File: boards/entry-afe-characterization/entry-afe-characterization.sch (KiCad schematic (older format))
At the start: 0 parts

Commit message: Continued design of entry-afe-characterization
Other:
- note added: "SYSTEM GAIN CALCULATIONS\n\nHMCAD1520 wants 2V full scale\nIn 12-bit mode: 488 µV/LSB @ 0 dB gain\nIn 8-bit mode: 7.8 mV/LSB @ 0 dB gain\n\nMIN GAIN:\n10V input range, -13 dB system gain (0.2V/V)\n-9 dB gain on VGA\n12 bit mode: 2.4 mV/LSB\n8 bit mode: 39 mV/LSB\n\nMAX GAIN:\n159 mV input range, +22 dB system gain (12.59V/V)\n+26 dB gain on VGA\n12 bit mode: 38.7 µV/LSB\n8 bit mode: 619.5 µV/LSB"
- note added: "VGAIN\n2.5V CM\nNet gain = 0.177 - 10 V/V\n-15 to +20 dB"
- note added: "VOUT\n900 mV CM\nNet gain = 0.223 - 12.59 V/V\n-13 to +22 dB"
- note removed: "SYSTEM GAIN CALCULATIONS\n\nHMCAD1520 wants 2V full scale\nIn 12-bit mode: 488 µV/LSB @ 0 dB gain\nIn 8-bit mode: 7.8 mV/LSB @ 0 dB gain\n\nMIN GAIN:\n10V input range, -13 dB system gain (0.2V/V)\n+2 dB gain on VGA\n12 bit mode: 2.4 mV/LSB\n8 bit mode: 39 mV/LSB\n\nMAX GAIN:\n502 mV input range, +12 dB system gain (3.98V/V)\n+26 dB gain on VGA\n12 bit mode: 122.6 µV/LSB\n8 bit mode: 1.95 mV/LSB"
- note removed: "VGAIN\n2.25V CM\nNet gain = 0.177 - 10 V/V\n-15 to +20 dB"
- note removed: "VOUT\n895 mV CM\nNet gain = 0.071 - 3.98 V/V\n-23 to +12 dB"
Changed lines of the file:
@@
 $EndSheet
 Text Notes 6350 3850 0    50   ~ 0
-SYSTEM GAIN CALCULATIONS\n\nHMCAD1520 wants 2V full scale\nIn 12-bit mode: 488 µV/LSB @ 0 dB gain\nIn 8-bit mode: 7.8 mV/LSB @ 0 dB gain\n\nMIN GAIN:\n10V input range, -13 dB system gain (0.2V/V)\n+2 dB gain on VGA\n12 bit mode: 2.4 mV/LSB\n8 bit mode: 39 mV/LSB\n\nMAX GAIN:\n502 mV input range, +12 dB system gain (3.98V/V)\n+26 dB gain on VGA\n12 bit mode: 122.6 µV/LSB\n8 bit mode: 1.95 mV/LSB
+SYSTEM GAIN CALCULATIONS\n\nHMCAD1520 wants 2V full scale\nIn 12-bit mode: 488 µV/LSB @ 0 dB gain\nIn 8-bit mode: 7.8 mV/LSB @ 0 dB gain\n\nMIN GAIN:\n10V input range, -13 dB system gain (0.2V/V)\n-9 dB gain on VGA\n12 bit mode: 2.4 mV/LSB\n8 bit mode: 39 mV/LSB\n\nMAX GAIN:\n159 mV input range, +22 dB system gain (12.59V/V)\n+26 dB gain on VGA\n12 bit mode: 38.7 µV/LSB\n8 bit mode: 619.5 µV/LSB
 $Sheet
 S 3900 5500 650  1750
@@
 F5 "VGAIN_P" O R 5650 750 50
 F6 "VGAIN_N" O R 5650 850 50
-F7 "2V25_REF" I L 4500 1150 50
+F7 "2V5_REF" I L 4500 1150 50
 $EndSheet
 Wire Wire Line
@@
 VSHIFTED\n0-5V range, 2.5V CM\nNet gain = 0.5V/V (-6 dB)\nVIN_OFFSET is ± 2.5V range
 Text Notes 4500 2050 0    50   ~ 0
-VGAIN\n2.25V CM\nNet gain = 0.177 - 10 V/V\n-15 to +20 dB
+VGAIN\n2.5V CM\nNet gain = 0.177 - 10 V/V\n-15 to +20 dB
 Text Label 4500 1150 2    50   ~ 0
-2V25_REF
+2V5_REF
 $Sheet
 S 6350 650  950  950
@@
 F2 "VGAIN_P" I L 6350 750 50
 F3 "VGAIN_N" I L 6350 850 50
-F4 "GND" I L 6350 1050 50
-F6 "VOUT_P" O R 7300 750 50
-F7 "VOUT_N" O R 7300 850 50
+F4 "GND" I L 6350 1150 50
+F5 "VOUT_P" O R 7300 750 50
+F6 "VOUT_N" O R 7300 850 50
+F7 "0V9_REF" I L 6350 1050 50
 $EndSheet
 Wire Wire Line
@@
 Wire Wire Line
 	5650 850  6350 850
-Text Label 6350 1050 2    50   ~ 0
+Text Label 6350 1150 2    50   ~ 0
 GND
 Text Notes 6350 2050 0    50   ~ 0
-VOUT\n895 mV CM\nNet gain = 0.071 - 3.98 V/V\n-23 to +12 dB
+VOUT\n900 mV CM\nNet gain = 0.223 - 12.59 V/V\n-13 to +22 dB
+Text Label 6350 1050 2    50   ~ 0
+0V9_REF
 $EndSCHEMATC

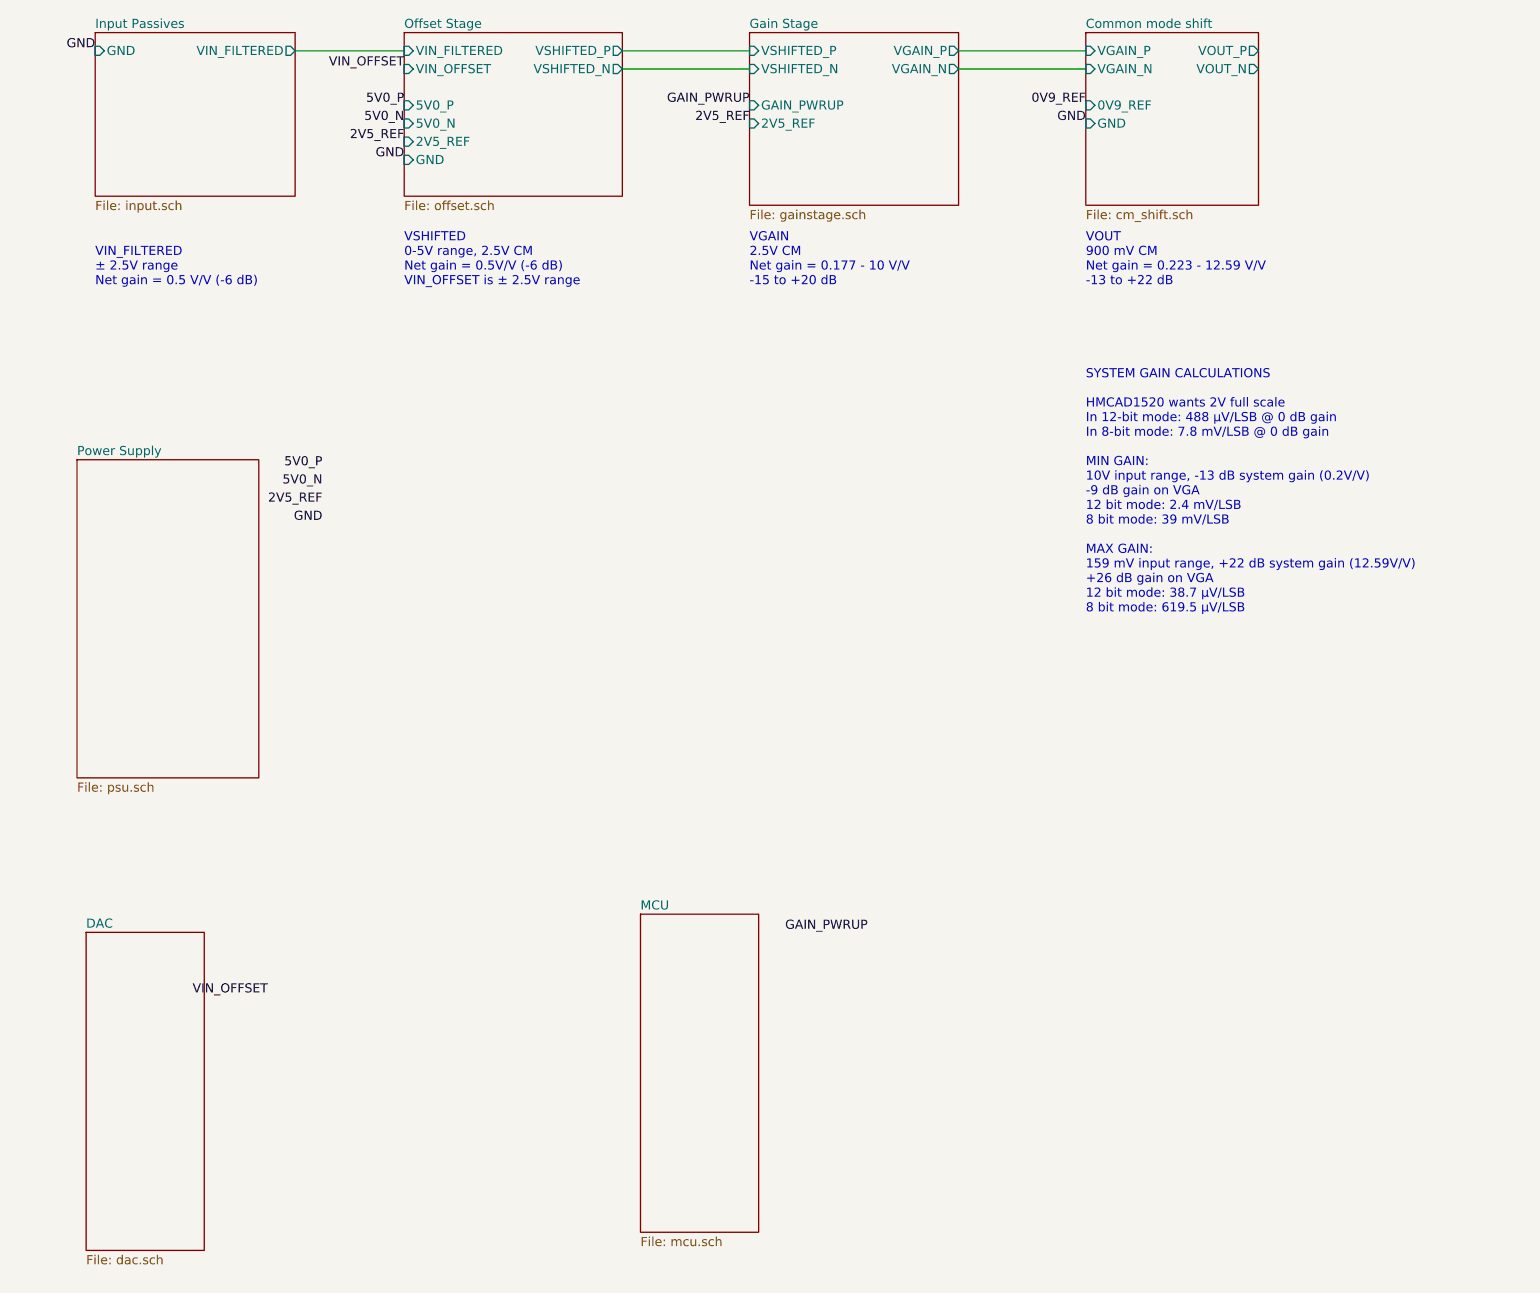
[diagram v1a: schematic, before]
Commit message: Continued work on AFE characterization board
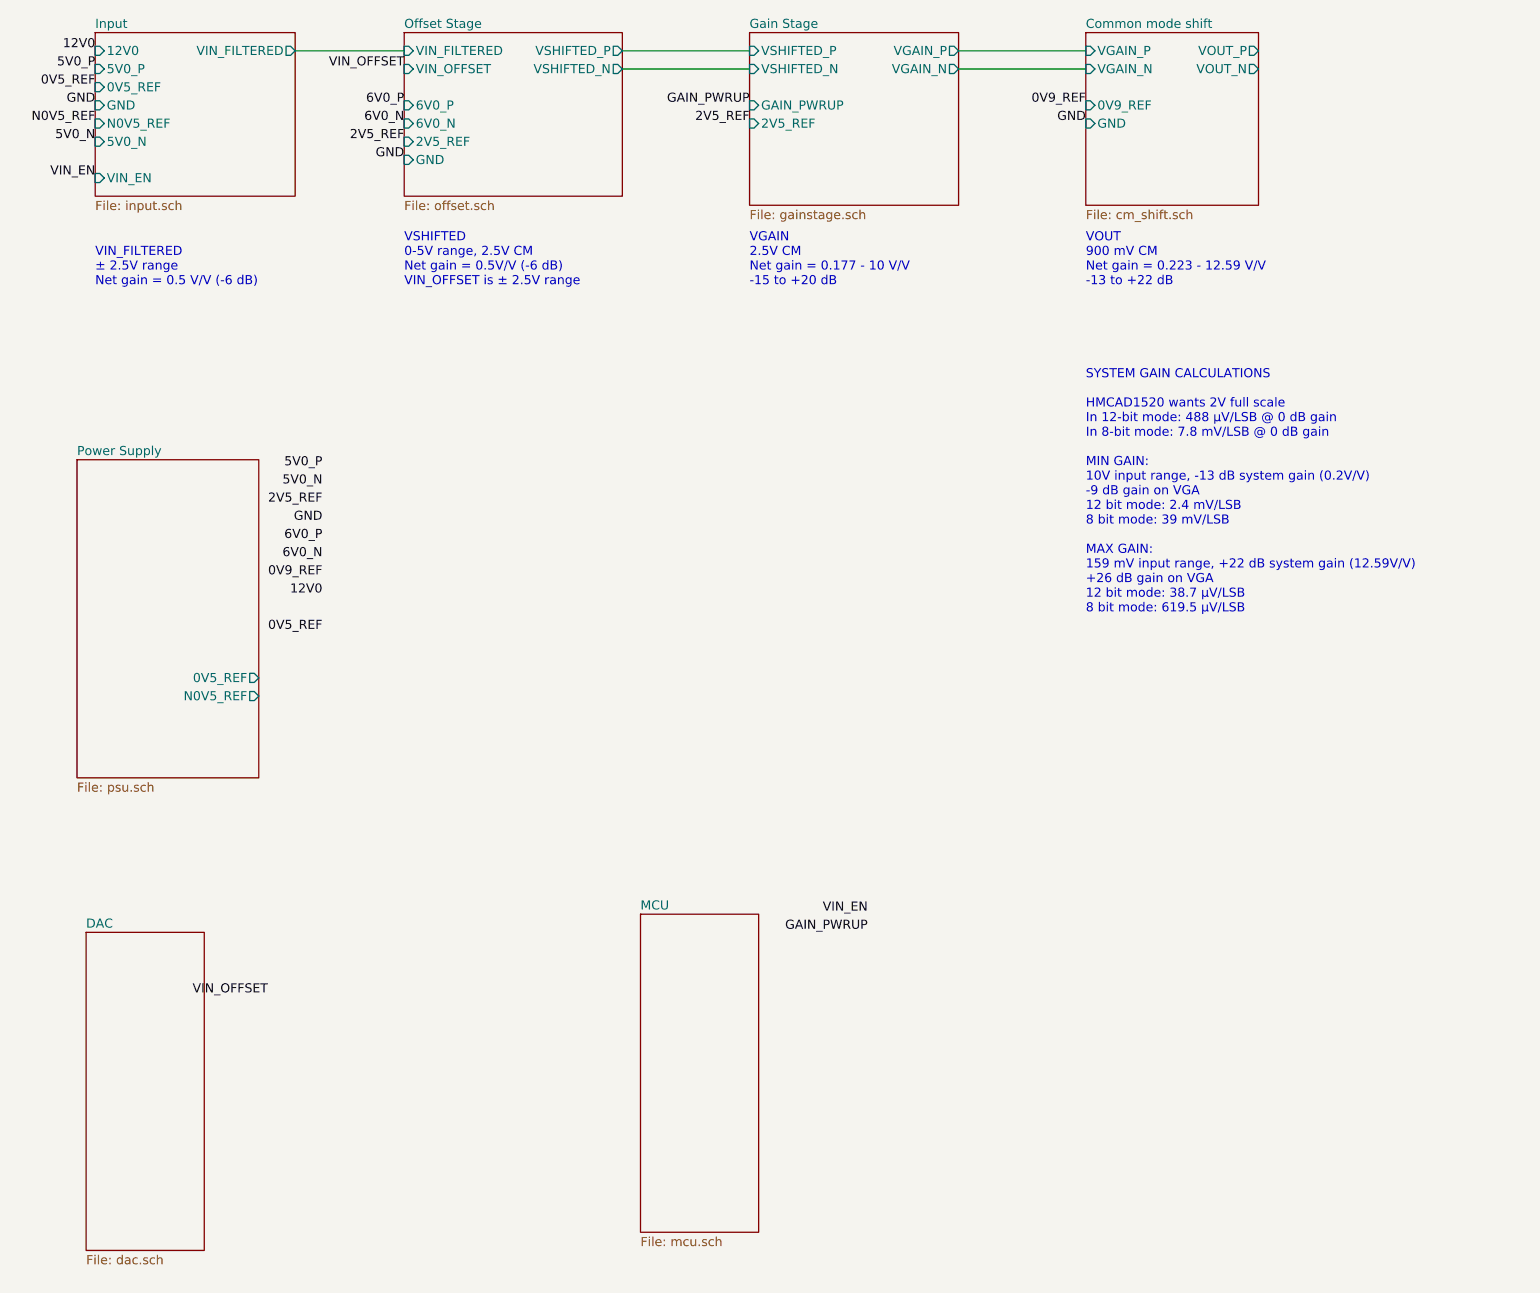
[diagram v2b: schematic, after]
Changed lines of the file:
@@
 EESchema Schematic File Version 4
+LIBS:entry-afe-characterization-cache
 EELAYER 30 0
 EELAYER END
@@
 Sheet 1 8
 Title "Entry-Level Oscilloscope AFE Characterization Platform"
-Date "2020-03-16"
+Date "2020-03-17"
 Rev "0.1"
 Comp "Antikernel Labs"
@@
 F0 "Power Supply" 50
 F1 "psu.sch" 50
+F2 "0V5_REF" O R 1800 4200 50
+F3 "N0V5_REF" O R 1800 4300 50
 $EndSheet
 $Sheet
@@
 S 900  650  1100 900
 U 5E7383DD
-F0 "Input Passives" 50
+F0 "Input" 50
 F1 "input.sch" 50
-F2 "GND" I L 900 750 50
+F2 "GND" I L 900 1050 50
 F3 "VIN_FILTERED" O R 2000 750 50
+F4 "VIN_EN" I L 900 1450 50
+F5 "5V0_P" I L 900 850 50
+F6 "5V0_N" I L 900 1250 50
+F7 "12V0" I L 900 750 50
+F8 "0V5_REF" I L 900 950 50
+F9 "N0V5_REF" I L 900 1150 50
 $EndSheet
-Text Label 900  750  2    50   ~ 0
+Text Label 900  1050 2    50   ~ 0
 GND
 $Sheet
@@
 F4 "VSHIFTED_P" O R 3800 750 50
 F5 "VSHIFTED_N" O R 3800 850 50
-F6 "5V0_P" I L 2600 1050 50
-F7 "5V0_N" I L 2600 1150 50
-F8 "GND" I L 2600 1350 50
-F9 "2V5_REF" I L 2600 1250 50
+F6 "GND" I L 2600 1350 50
+F7 "2V5_REF" I L 2600 1250 50
+F8 "6V0_P" I L 2600 1050 50
+F9 "6V0_N" I L 2600 1150 50
 $EndSheet
 Text Label 2600 850  2    50   ~ 0
@@
 Wire Wire Line
 	2000 750  2600 750
-Text Label 2600 1050 2    50   ~ 0
-5V0_P
-Text Label 2600 1150 2    50   ~ 0
-5V0_N
 Text Label 2600 1350 2    50   ~ 0
 GND
@@
 Text Label 6350 1050 2    50   ~ 0
 0V9_REF
+Text Label 2600 1050 2    50   ~ 0
+6V0_P
+Text Label 2600 1150 2    50   ~ 0
+6V0_N
+Text Label 2150 3450 2    50   ~ 0
+6V0_P
+Text Label 2150 3550 2    50   ~ 0
+6V0_N
+Text Label 2150 3650 2    50   ~ 0
+0V9_REF
+Text Label 5150 5500 2    50   ~ 0
+VIN_EN
+Text Label 900  1450 2    50   ~ 0
+VIN_EN
+Text Label 900  850  2    50   ~ 0
+5V0_P
+Text Label 900  1250 2    50   ~ 0
+5V0_N
+Text Label 900  750  2    50   ~ 0
+12V0
+Text Label 2150 3750 2    50   ~ 0
+12V0
+Text Label 2150 3950 2    50   ~ 0
+0V5_REF
+Text Label 900  1150 2    50   ~ 0
+N0V5_REF
+Text Label 900  950  2    50   ~ 0
+0V5_REF
 $EndSCHEMATC

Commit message: Continued work on AFE characterization board. Still have to do power supply.
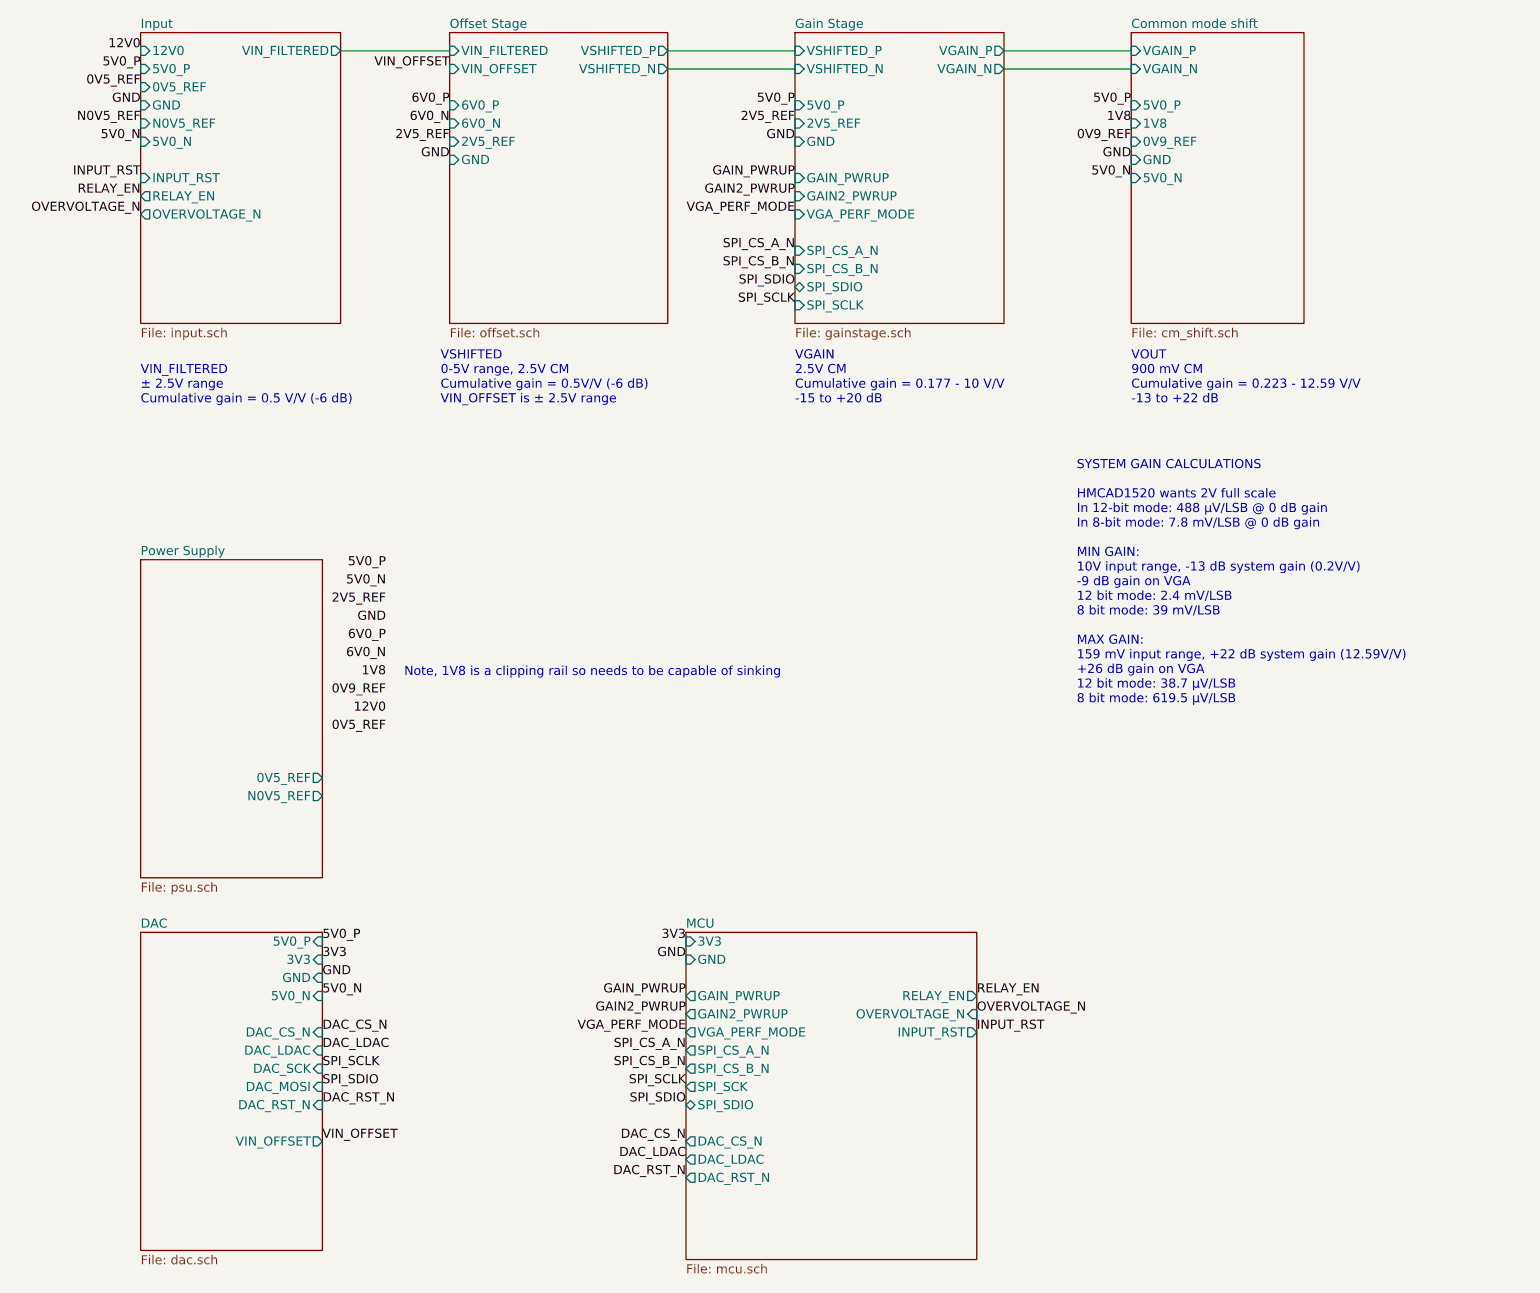
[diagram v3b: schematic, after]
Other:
- note added: "Note, 1V8 is a clipping rail so needs to be capable of sinking"
- note added: "VGAIN\n2.5V CM\nCumulative gain = 0.177 - 10 V/V\n-15 to +20 dB"
- note added: "VIN_FILTERED\n± 2.5V range\nCumulative gain = 0.5 V/V (-6 dB)"
- note added: "VOUT\n900 mV CM\nCumulative gain = 0.223 - 12.59 V/V\n-13 to +22 dB"
- note added: "VSHIFTED\n0-5V range, 2.5V CM\nCumulative gain = 0.5V/V (-6 dB)\nVIN_OFFSET is ± 2.5V range"
- note removed: "VGAIN\n2.5V CM\nNet gain = 0.177 - 10 V/V\n-15 to +20 dB"
- note removed: "VIN_FILTERED\n± 2.5V range\nNet gain = 0.5 V/V (-6 dB)"
- note removed: "VOUT\n900 mV CM\nNet gain = 0.223 - 12.59 V/V\n-13 to +22 dB"
- note removed: "VSHIFTED\n0-5V range, 2.5V CM\nNet gain = 0.5V/V (-6 dB)\nVIN_OFFSET is ± 2.5V range"
